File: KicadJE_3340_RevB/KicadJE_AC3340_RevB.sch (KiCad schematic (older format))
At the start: 146 parts, among them J101 RampOut1, J102 PulseOut2, J103 SawOut3, J104 In1.1, J105 In1.2, J106 In1.3, J107 SS_In2, J108 HS_In3, J109 FM_In4, J110 PWM_In5, J111 SineOut4, P101 HEADER_2x5_Doepfer, Q101 MMBT3906, Q102 UMX1N, SW101 Octave (3 state), U101 TL072, U102 TL072, U103 TL072, U104 AS3340, U105 L78L05_SOT89, U106 L79L05_SOT89, U107 TL072

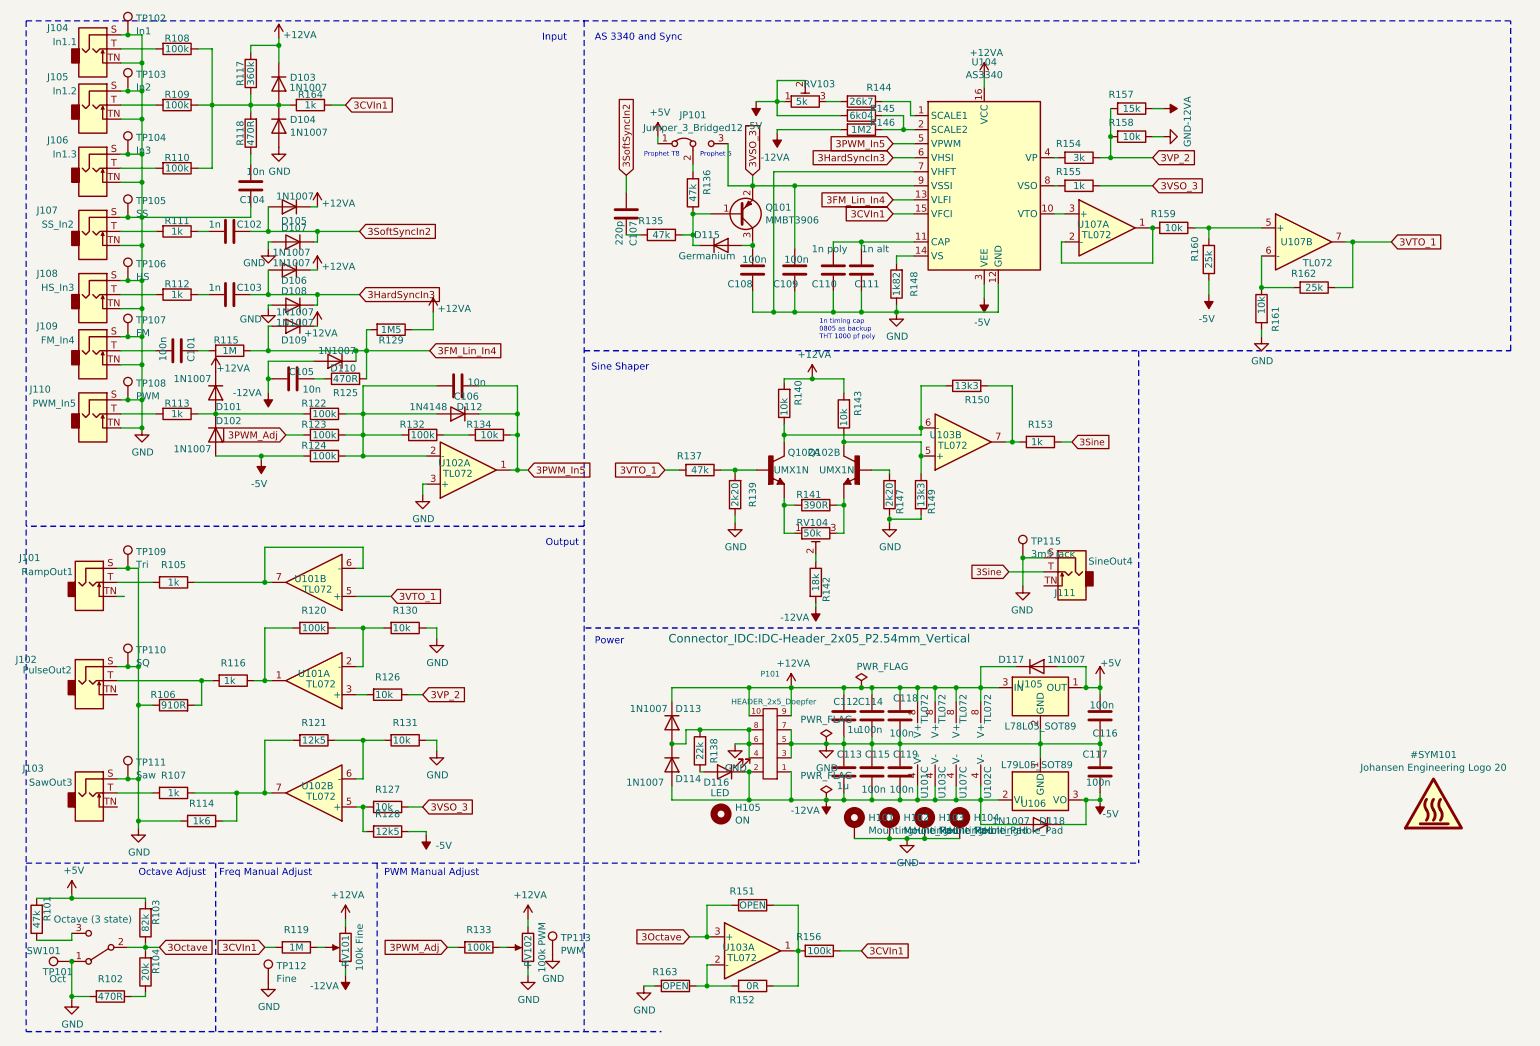
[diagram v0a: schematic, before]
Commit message: Update KicadJE_AC3340_RevB.sch
Fix misc errata from RevA - not complete
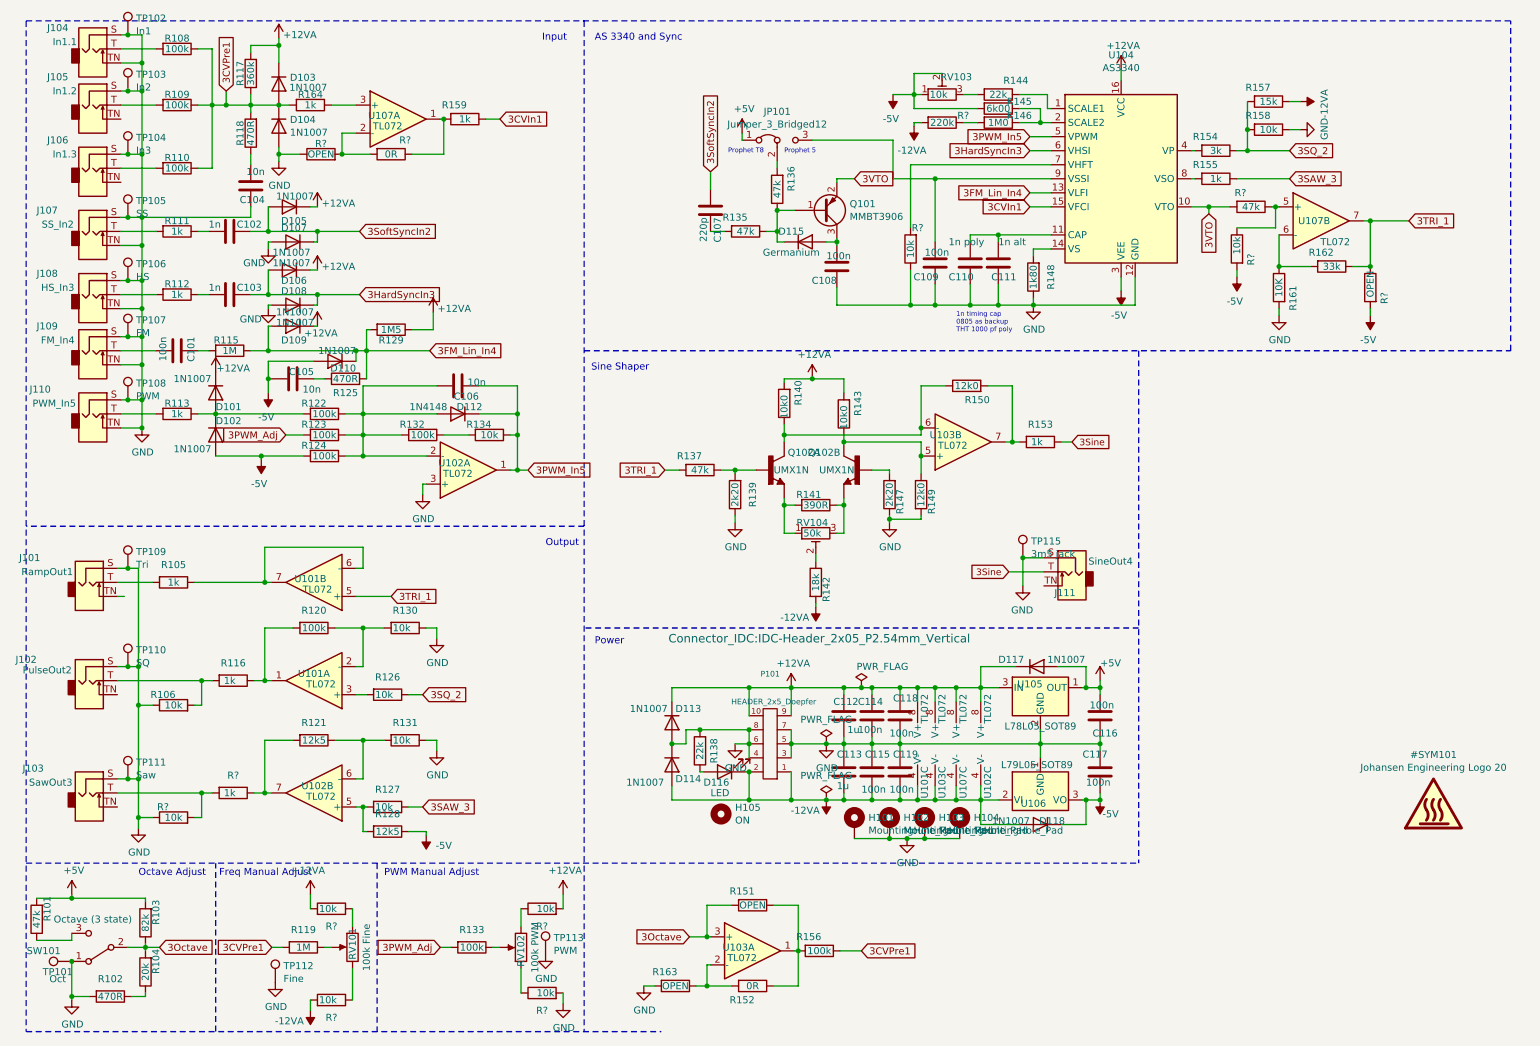
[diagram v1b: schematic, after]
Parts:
- removed R107: 1k, Resistor_SMD:R_0805_2012Metric_Pad1.15x1.40mm_HandSolder, symbol Device:R
- removed R114: 1k6, Resistor_SMD:R_0805_2012Metric_Pad1.15x1.40mm_HandSolder, symbol Device:R
- removed R160: 25k, Resistor_SMD:R_0805_2012Metric_Pad1.15x1.40mm_HandSolder, symbol Device:R
- added R? (x7): 10k, Resistor_SMD:R_0805_2012Metric_Pad1.15x1.40mm_HandSolder, symbol Device:R
- added R?: 0R, Resistor_SMD:R_0805_2012Metric_Pad1.15x1.40mm_HandSolder, symbol Device:R
- added R? (x2): OPEN, Resistor_SMD:R_0805_2012Metric_Pad1.15x1.40mm_HandSolder, symbol Device:R
- added R?: 47k, Resistor_SMD:R_0805_2012Metric_Pad1.15x1.40mm_HandSolder, symbol Device:R
- added R?: 220k, Resistor_SMD:R_0805_2012Metric_Pad1.15x1.40mm_HandSolder, symbol Device:R
- added R?: 1k, Resistor_SMD:R_0805_2012Metric_Pad1.15x1.40mm_HandSolder, symbol Device:R
- R106: value 910R -> 10k
- R140, R143: value 10k -> 10k0
- R144: value 26k7 -> 22k
- R145: value 6k04 -> 6k00
- R146: value 1M2 -> 1M0
- R148: value 1k82 -> 1k80
- R149, R150: value 13k3 -> 12k0
- R159: value 10k -> 1k
- R161: value 10k -> 10K
- R162: value 25k -> 33k
- RV103: value 5k -> 10k
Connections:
- net +12VA: now also R?.2, R?.2; no longer RV101.3, RV102.3
- net -12VA: now also R?.2, R?.2; no longer C105.1, D110.2 (A), R146.2, RV101.1
- net -5V: now also C105.1, D110.2 (A), R?.2, R?.2
- net 3CVIn1: now also R159.1; no longer R119.2, R156.1, R164.1
- net GND: now also R?.1, R?.1, R?.1, R?.2; no longer J105.TN, J106.TN, RV102.1, U104.7 (VHFT)
- net 3CVPre1: now reaches D103.2 (A), D104.1 (K), R108.1, R109.1, R110.1, R117.1, R118.2, R164.2
- net 3CVPre1: now also R119.2, R156.1
- net at J103.T: now also R?.2, R?.2
- net at R121.2, U102.7: now also R?.1
- net at U107.3 (+): now also R164.1; no longer U104.10 (VTO)
- net at R159.2, U107.1: now also R?.1; no longer U107.2 (-)
- net at U107.5 (+): now also R?.1, R?.1; no longer R159.1
- net 3VP_2 renamed 3SQ_2
- net 3VSO_3: no longer names the net of C109.2, JP101.3 (B), U104.9 (VSSI)
- net 3VSO_3: no longer Q101.2 (E), R127.1, R155.1
- net 3VTO_1 renamed 3TRI_1
- net 3TRI_1: now also R?.1
- new net: R?.1, RV102.3
- new net: R?.1, RV102.1
- new net: R?.1, RV101.3
- new net: R?.1, RV101.1
- new net: R?.2, R?.2, U107.2 (-)
- new net: R?.2, U104.7 (VHFT)
- new net: R146.2, R?.1
- new net 3SAW_3: R127.1, R155.1
- new net 3VTO: Q101.2 (E), R?.2, U104.10 (VTO)
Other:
- moved on the sheet: C107, C108, C109, C110, C111, D115, JP101, Q101, R119, R133, R135, R136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

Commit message: Update KicadJE_AC3340_RevB.sch
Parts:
- removed R151: OPEN, Resistor_SMD:R_0805_2012Metric_Pad1.15x1.40mm_HandSolder, symbol Device:R
- added R? (x2): 0R, Resistor_SMD:R_0805_2012Metric_Pad1.15x1.40mm_HandSolder, symbol Device:R
- added R? (x2): OPEN, Resistor_SMD:R_0805_2012Metric_Pad1.15x1.40mm_HandSolder, symbol Device:R
- R121, R128: value 12k5 -> 12k0
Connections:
- net -5V: now also R?.1
- net 3TRI_1: now also R?.1; no longer U101.5 (+)
- net GND: now also R?.1
- net at R105.1, U101.7: now also R?.2; no longer U101.6 (-)
- new net: R?.2, R?.2, U101.5 (+)
- new net: R?.1, R?.2, U101.6 (-)
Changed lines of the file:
@@
 Text GLabel 3350 6125 2    50   Input ~ 0
 3SAW_3
-Text GLabel 3125 4625 2    50   Input ~ 0
+Text GLabel 3550 4450 2    50   Input ~ 0
 3TRI_1
 Text GLabel 3350 5325 2    50   Input ~ 0
@@
 Wire Wire Line
 	2875 4425 2925 4425
-Wire Wire Line
-	2925 4425 2925 4275
-Wire Wire Line
-	2925 4275 2225 4275
-Wire Wire Line
-	2225 4275 2225 4525
 Connection ~ 2225 4525
 Wire Wire Line
@@
 AR Path="/5F49A670/5FE7E2FE" Ref="R?"  Part="1"
 F 0 "R121" V 2450 5650 50  0000 C CNN
-F 1 "12k5" V 2575 5650 50  0000 C CNN
+F 1 "12k0" V 2575 5650 50  0000 C CNN
 F 2 "Resistor_SMD:R_0805_2012Metric_Pad1.15x1.40mm_HandSolder" V 2505 5650 50  0001 C CNN
 F 3 "~" H 2575 5650 50  0001 C CNN
@@
 AR Path="/5F49A670/5FEC766A" Ref="R?"  Part="1"
 F 0 "R128" V 2975 6300 50  0000 C CNN
-F 1 "12k5" V 3100 6300 50  0000 C CNN
+F 1 "12k0" V 3100 6300 50  0000 C CNN
 F 2 "Resistor_SMD:R_0805_2012Metric_Pad1.15x1.40mm_HandSolder" V 3030 6300 50  0001 C CNN
 F 3 "~" H 3100 6300 50  0001 C CNN
@@
 	2400 1125 2325 1125
 $Comp
-L Device:R R151
-U 1 1 61551447
-P 5700 6825
-AR Path="/61551447" Ref="R151"  Part="1"
-AR Path="/5C8C5FC0/61551447" Ref="R?"  Part="1"
-AR Path="/5CAAE8D3/61551447" Ref="R?"  Part="1"
-AR Path="/5E4B0DD9/61551447" Ref="R?"  Part="1"
-AR Path="/5E62ACA1/61551447" Ref="R?"  Part="1"
-AR Path="/5F49A670/61551447" Ref="R?"  Part="1"
-F 0 "R151" V 5600 6750 50  0000 C CNN
-F 1 "OPEN" V 5700 6825 50  0000 C CNN
-F 2 "Resistor_SMD:R_0805_2012Metric_Pad1.15x1.40mm_HandSolder" V 5630 6825 50  0001 C CNN
-F 3 "~" H 5700 6825 50  0001 C CNN
-	1    5700 6825
-	0    1    1    0
-$EndComp
-Wire Wire Line
-	5375 7050 5375 6825
-Wire Wire Line
-	5375 6825 5550 6825
-Wire Wire Line
-	5375 7050 5400 7050
-Wire Wire Line
-	6025 7150 6025 6825
-Wire Wire Line
-	6025 6825 5850 6825
-$Comp
 L Envelope-cache-2018-08-04-13-00-04:GND #PWR0125
 U 1 1 615A670C
@@
 Text GLabel 5250 7050 0    50   Input ~ 0
 3Octave
-Wire Wire Line
-	5250 7050 5375 7050
-Connection ~ 5375 7050
 $Comp
 L Device:R R163
@@
 	6300 2550 6300 2425
 Connection ~ 6825 2550
+$Comp
+L Device:R R?
+U 1 1 5F77C881
+P 3300 4450
+AR Path="/5F77C881" Ref="R?"  Part="1"
+AR Path="/5C8C5FC0/5F77C881" Ref="R?"  Part="1"
+AR Path="/5CAAE8D3/5F77C881" Ref="R?"  Part="1"
+AR Path="/5E4B0DD9/5F77C881" Ref="R?"  Part="1"
+AR Path="/5F49A670/5F77C881" Ref="R?"  Part="1"
+F 0 "R?" V 3175 4450 50  0000 C CNN
+F 1 "0R" V 3300 4425 50  0000 C CNN
+F 2 "Resistor_SMD:R_0805_2012Metric_Pad1.15x1.40mm_HandSolder" V 3230 4450 50  0001 C CNN
+F 3 "~" H 3300 4450 50  0001 C CNN
+	1    3300 4450
+	0    1    1    0
+$EndComp
+Wire Wire Line
+	3450 4450 3550 4450
+$Comp
+L Device:R R?
+U 1 1 5F77C88C
+P 3300 4625
+AR Path="/5F77C88C" Ref="R?"  Part="1"
+AR Path="/5C8C5FC0/5F77C88C" Ref="R?"  Part="1"
+AR Path="/5CAAE8D3/5F77C88C" Ref="R?"  Part="1"
+AR Path="/5E4B0DD9/5F77C88C" Ref="R?"  Part="1"
+AR Path="/5F49A670/5F77C88C" Ref="R?"  Part="1"
+F 0 "R?" V 3175 4625 50  0000 C CNN
+F 1 "OPEN" V 3300 4625 50  0000 C CNN
+F 2 "Resistor_SMD:R_0805_2012Metric_Pad1.15x1.40mm_HandSolder" V 3230 4625 50  0001 C CNN
+F 3 "~" H 3300 4625 50  0001 C CNN
+	1    3300 4625
+	0    1    1    0
+$EndComp
+Wire Wire Line
+	3150 4625 3125 4625
+Wire Wire Line
+	3125 4625 3125 4450
+Wire Wire Line
+	3125 4450 3150 4450
+$Comp
+L power:-5V #PWR?
+U 1 1 5F77C89A
+P 3575 4650
+AR Path="/5E62ACA1/5F77C89A" Ref="#PWR?"  Part="1"
+AR Path="/5F49A670/5F77C89A" Ref="#PWR?"  Part="1"
+AR Path="/5F77C89A" Ref="#PWR?"  Part="1"
+F 0 "#PWR?" H 3575 4750 50  0001 C CNN
+F 1 "-5V" H 3450 4725 50  0000 C CNN
+F 2 "" H 3575 4650 50  0001 C CNN
+F 3 "" H 3575 4650 50  0001 C CNN
+	1    3575 4650
+	-1   0    0    1
+$EndComp
+Wire Wire Line
+	3575 4650 3575 4625
+Wire Wire Line
+	3575 4625 3450 4625
+Connection ~ 3125 4625
+Wire Wire Line
+	2925 4200 2725 4200
+$Comp
+L Device:R R?
+U 1 1 5F85F1F1
+P 2575 4200
+AR Path="/5F85F1F1" Ref="R?"  Part="1"
+AR Path="/5C8C5FC0/5F85F1F1" Ref="R?"  Part="1"
+AR Path="/5CAAE8D3/5F85F1F1" Ref="R?"  Part="1"
+AR Path="/5E4B0DD9/5F85F1F1" Ref="R?"  Part="1"
+AR Path="/5F49A670/5F85F1F1" Ref="R?"  Part="1"
+F 0 "R?" V 2450 4200 50  0000 C CNN
+F 1 "0R" V 2575 4200 50  0000 C CNN
+F 2 "Resistor_SMD:R_0805_2012Metric_Pad1.15x1.40mm_HandSolder" V 2505 4200 50  0001 C CNN
+F 3 "~" H 2575 4200 50  0001 C CNN
+	1    2575 4200
+	0    1    1    0
+$EndComp
+Wire Wire Line
+	2425 4200 2225 4200
+$Comp
+L Device:R R?
+U 1 1 5F85F1FC
+P 3225 4200
+AR Path="/5F85F1FC" Ref="R?"  Part="1"
+AR Path="/5C8C5FC0/5F85F1FC" Ref="R?"  Part="1"
+AR Path="/5CAAE8D3/5F85F1FC" Ref="R?"  Part="1"
+AR Path="/5E4B0DD9/5F85F1FC" Ref="R?"  Part="1"
+AR Path="/5F49A670/5F85F1FC" Ref="R?"  Part="1"
+F 0 "R?" V 3100 4200 50  0000 C CNN
+F 1 "OPEN" V 3225 4175 50  0000 C CNN
+F 2 "Resistor_SMD:R_0805_2012Metric_Pad1.15x1.40mm_HandSolder" V 3155 4200 50  0001 C CNN
+F 3 "~" H 3225 4200 50  0001 C CNN
+	1    3225 4200
+	0    1    1    0
+$EndComp
+Wire Wire Line
+	2925 4200 3075 4200
+Connection ~ 2925 4200
+$Comp
+L Envelope-cache-2018-08-04-13-00-04:GND #PWR?
+U 1 1 5F85F208
+P 3450 4275
+AR Path="/5F85F208" Ref="#PWR?"  Part="1"
+AR Path="/5C8C5FC0/5F85F208" Ref="#PWR?"  Part="1"
+AR Path="/5CAAE8D3/5F85F208" Ref="#PWR?"  Part="1"
+AR Path="/5E4B0DD9/5F85F208" Ref="#PWR?"  Part="1"
+AR Path="/5F49A670/5F85F208" Ref="#PWR?"  Part="1"
+F 0 "#PWR?" H 3450 4025 50  0001 C CNN
+F 1 "GND" H 3455 4102 50  0000 C CNN
+F 2 "" H 3450 4275 50  0001 C CNN
+F 3 "" H 3450 4275 50  0001 C CNN
+	1    3450 4275
+	1    0    0    -1
+$EndComp
+Wire Wire Line
+	3450 4275 3450 4200
+Wire Wire Line
+	3450 4200 3375 4200
+Wire Wire Line
+	2925 4200 2925 4425
+Wire Wire Line
+	2225 4200 2225 4525
+Wire Wire Line
+	5250 7050 5400 7050
 $EndSCHEMATC

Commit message: Update KicadJE_AC3340_RevB.sch
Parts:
- added R?: 0R, Resistor_SMD:R_0805_2012Metric_Pad1.15x1.40mm_HandSolder, symbol Device:R
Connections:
- net +5V: now also R?.2; no longer R103.2
- new net: R103.2, R?.1
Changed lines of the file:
@@
 	1375 6800 1375 6775
 Wire Wire Line
-	1375 6775 850  6775
+	1375 6775 1275 6775
 Wire Wire Line
 	850  6775 850  6750
@@
 Wire Wire Line
 	5250 7050 5400 7050
+$Comp
+L Device:R R?
+U 1 1 5F8D56CF
+P 1125 6775
+AR Path="/5F8D56CF" Ref="R?"  Part="1"
+AR Path="/5C8C5FC0/5F8D56CF" Ref="R?"  Part="1"
+AR Path="/5CAAE8D3/5F8D56CF" Ref="R?"  Part="1"
+AR Path="/5E4B0DD9/5F8D56CF" Ref="R?"  Part="1"
+AR Path="/5F49A670/5F8D56CF" Ref="R?"  Part="1"
+F 0 "R?" V 1000 6775 50  0000 C CNN
+F 1 "0R" V 1125 6775 50  0000 C CNN
+F 2 "Resistor_SMD:R_0805_2012Metric_Pad1.15x1.40mm_HandSolder" V 1055 6775 50  0001 C CNN
+F 3 "~" H 1125 6775 50  0001 C CNN
+	1    1125 6775
+	0    1    1    0
+$EndComp
+Wire Wire Line
+	975  6775 850  6775
 $EndSCHEMATC
